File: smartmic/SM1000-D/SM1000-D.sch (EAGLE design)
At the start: 197 parts, among them CN1 HDR100-3, CN10 ST-3509, CN11 HDR100-3, CN12 HRS-A3C-16DA, CN2 JS-MU3-002, CN3 DS-0518, CN4 RJ-45, CN5 ST-3509, CN6 ST-3509, CN7 ST-3509, CN8 ST-3509, CN9 ST-3509, J1 JMP-2PIN, J3 JMP-2PIN, J4 JMP-2PIN, P1 TPAD50, P10 TPAD50, P11 TPAD50, P12 TPAD50, P13 TPAD50, P14 TPAD50, P16 TPAD50, P18 TPAD50, P19 TPAD50, P2 TPAD50, P20 TPAD50, P3 TPAD50, P4 TPAD50, P5 TPAD50, P6 TPAD50, P7 TPAD50, P8 TPAD50, P9 TPAD50, SW1 TS-026, SW2 TS-026, SW3 DPDT, SW4 TS-026, SW5 TS-02B, T1 SM-LP-5001, T2 SM-LP-5001, U1 STM32F407, U2 LD3985M33R, U3 STMPS2141, U4 EMIF02-USB03F2, U5 TPS54329E, U6 LMV341, U7 LMV341, U8 LM386M-1, U9 LMV341

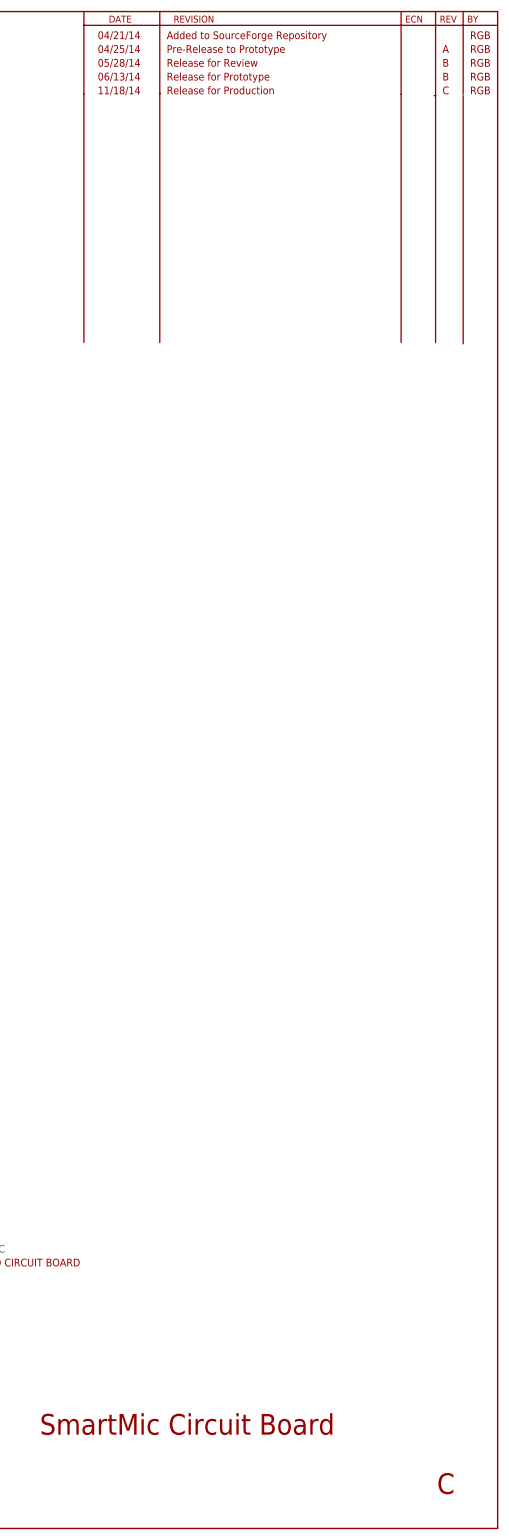
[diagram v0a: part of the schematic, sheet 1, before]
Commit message: Complete SM1000-C -> SM1000-D update RGB
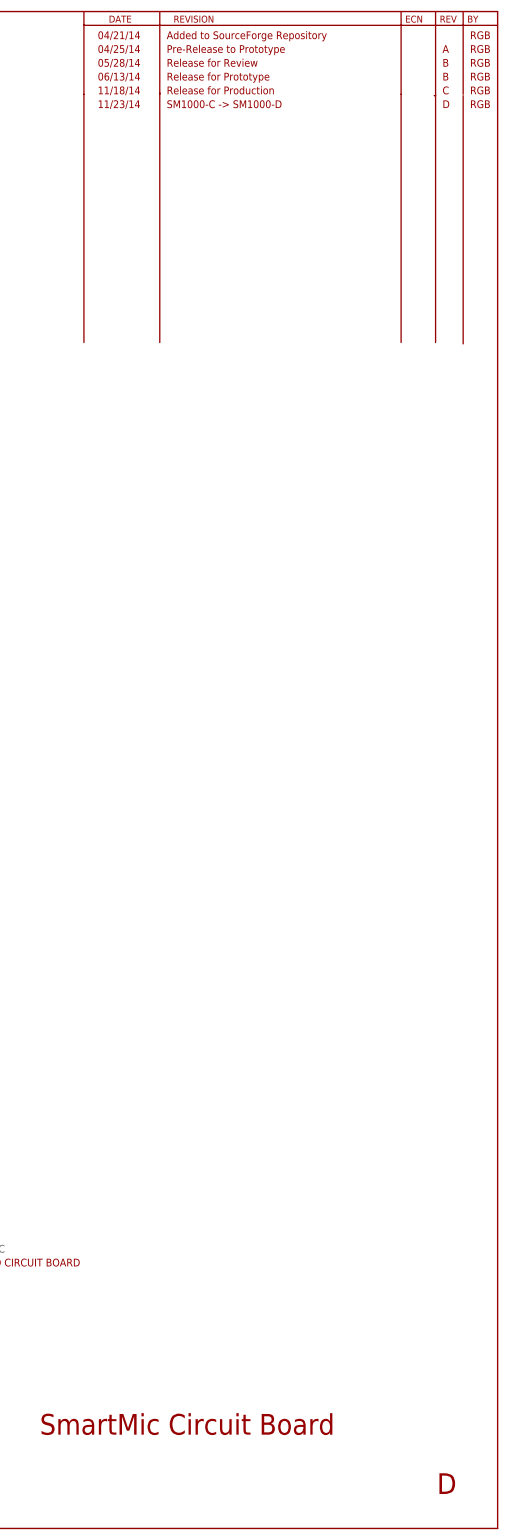
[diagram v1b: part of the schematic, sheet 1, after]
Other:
- note added: "11/23/14"
- note added: "D"
- note added: "SM1000-C -> SM1000-D"
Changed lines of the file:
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@@
 <text x="137.16" y="73.66" size="2.54" layer="94" ratio="10">STM32F407 PWR CIRCUIT</text>
 <text x="347.472" y="17.272" size="3.81" layer="94" ratio="10">SmartMic Circuit Board</text>
-<text x="420.624" y="6.35" size="3.81" layer="94" ratio="10">C</text>
+<text x="420.624" y="6.35" size="3.81" layer="94" ratio="10">D</text>
 <text x="358.14" y="274.32" size="1.4224" layer="94" ratio="10">04/21/14</text>
 <text x="370.84" y="274.32" size="1.4224" layer="94" ratio="10">Added to SourceForge Repository</text>
@@
 <text x="370.84" y="264.16" size="1.4224" layer="94" ratio="10">Release for Production</text>
 <text x="358.14" y="264.16" size="1.4224" layer="94" ratio="10">11/18/14</text>
+<text x="358.14" y="261.62" size="1.4224" layer="94" ratio="10">11/23/14</text>
+<text x="370.84" y="261.62" size="1.4224" layer="94" ratio="10">SM1000-C -&gt; SM1000-D</text>
+<text x="421.64" y="261.62" size="1.4224" layer="94" ratio="10">D</text>
+<text x="426.72" y="261.62" size="1.4224" layer="94" ratio="10">RGB</text>
 </plain>
 <instances>
@@
 <text x="220.98" y="193.04" size="2.54" layer="94" ratio="10">RIG INTERFACE</text>
 <text x="346.456" y="17.272" size="3.81" layer="94" ratio="10">Smart Mic Circuit Board</text>
-<text x="418.592" y="6.604" size="3.81" layer="94" ratio="10">C</text>
+<text x="418.592" y="6.604" size="3.81" layer="94" ratio="10">D</text>
 <text x="10.16" y="149.86" size="1.4224" layer="94" ratio="10">NORMAL - 1-2</text>
 <text x="10.16" y="147.32" size="1.4224" layer="94" ratio="10">OPT MIC - 1 ONLY,</text>
@@
 <text x="210.82" y="238.76" size="1.4224" layer="94" ratio="10" rot="R180">DNL</text>
 <wire x1="251.46" y1="45.72" x2="327.66" y2="45.72" width="0.1524" layer="94" style="longdash"/>
+<text x="355.6" y="264.16" size="1.4224" layer="94" ratio="10">11/23/14</text>
+<text x="368.3" y="264.16" size="1.4224" layer="94" ratio="10">SM1000-C -&gt; SM1000-D</text>
+<text x="419.1" y="264.16" size="1.4224" layer="94" ratio="10">D</text>
+<text x="424.18" y="264.16" size="1.4224" layer="94" ratio="10">RGB</text>
 </plain>
 <instances>

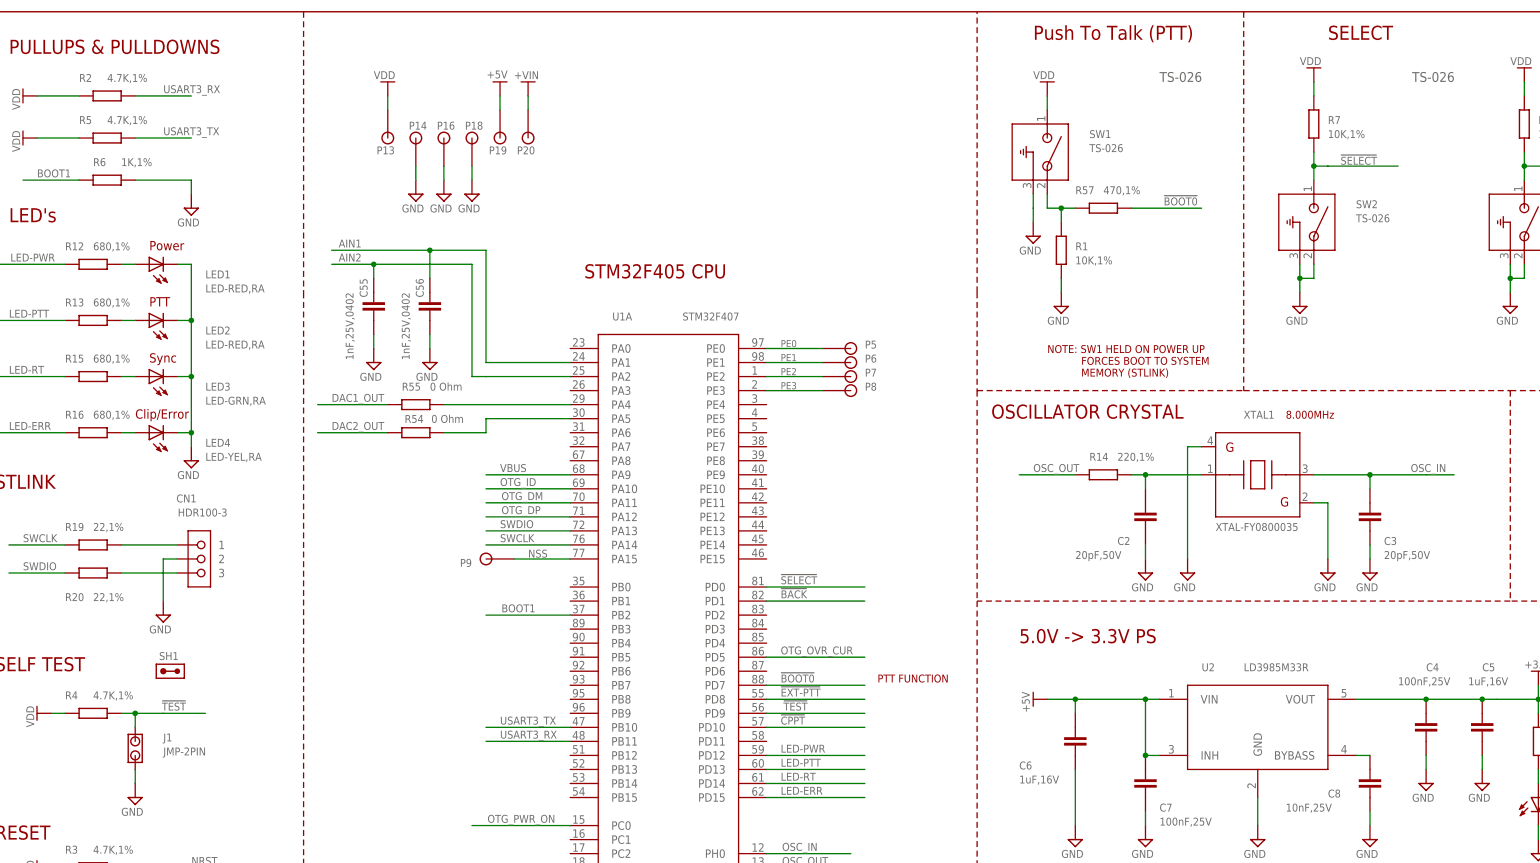
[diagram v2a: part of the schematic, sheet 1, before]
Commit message: Incorporated new PTT SW & TrimPOTs
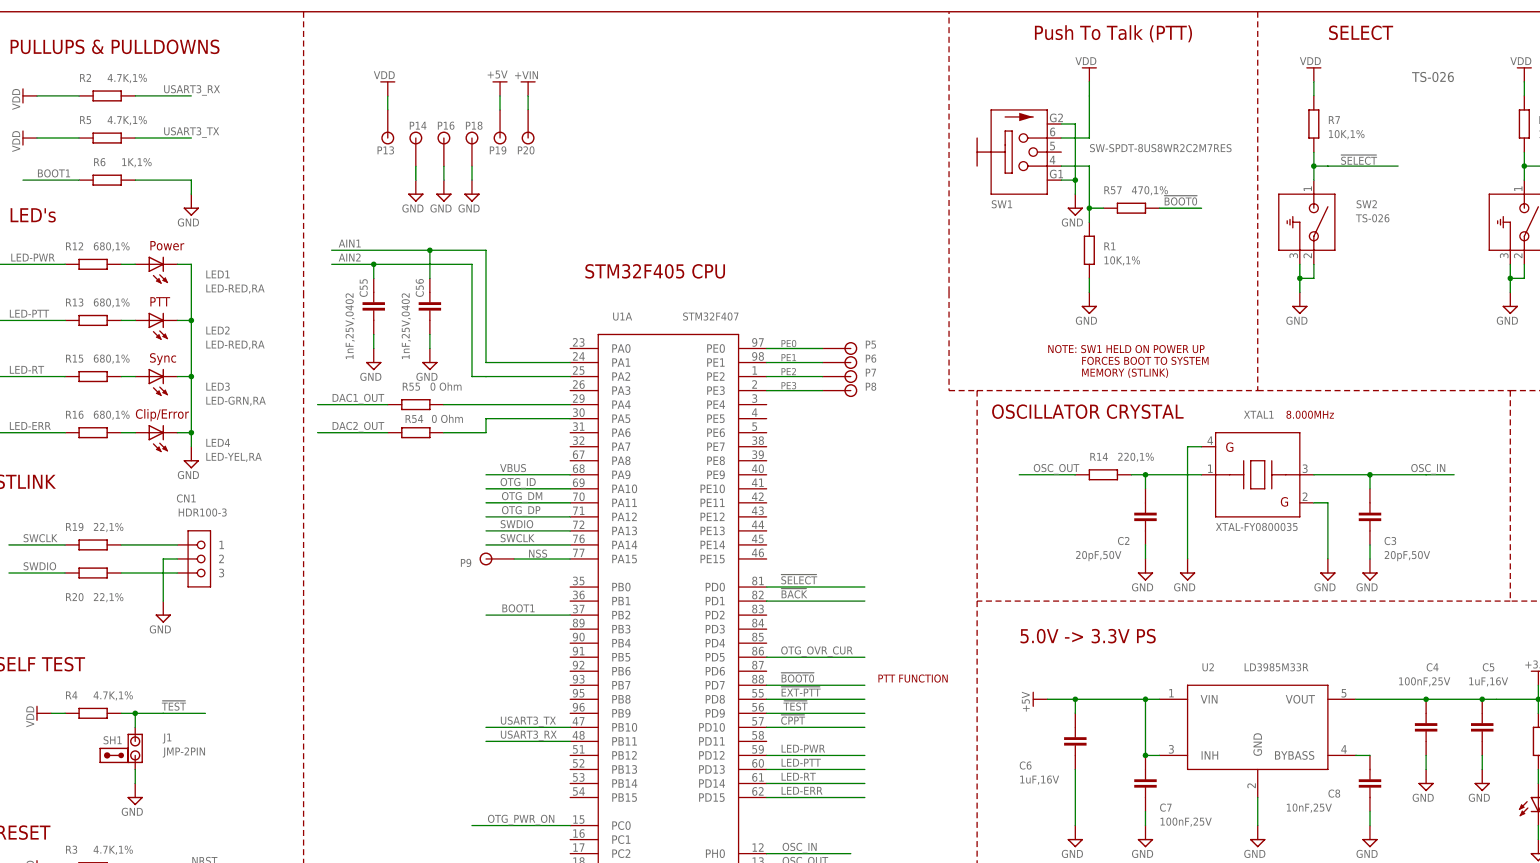
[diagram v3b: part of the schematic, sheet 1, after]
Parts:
- R42, R47, R52: device _RoweTel:PAN-EVM1D -> _RoweTel:POT3361
- SW1: value TS-026 -> SW-SPDT-8US8WR2C2M7RES; device _RoweTel:TS-026 -> _RoweTel:SW-SPDT-8US8WR2C2M7RES
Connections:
- net GND: now also SW1.G1, SW1.G2; no longer SW1.3
- net N$14: now also SW1.4; no longer SW1.2
- net VDD: now also SW1.6; no longer SW1.1
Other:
- moved on the sheet: R1, R57, SH1, SH3
